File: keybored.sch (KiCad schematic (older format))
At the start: 161 parts, among them J1 USB_C_Receptacle_USB2.0, K1 KEYSW, K10 KEYSW, K11 KEYSW, K12 KEYSW, K13 KEYSW, K14 KEYSW, K15 KEYSW, K16 KEYSW, K17 KEYSW, K18 KEYSW, K19 KEYSW, K2 KEYSW, K20 KEYSW, K21 KEYSW, K22 KEYSW, K23 KEYSW, K24 KEYSW, K25 KEYSW, K26 KEYSW, K27 KEYSW, K28 KEYSW, K29 KEYSW, K3 KEYSW, K30 KEYSW, K31 KEYSW, K32 KEYSW, K33 KEYSW, K34 KEYSW, K35 KEYSW, K36 KEYSW, K37 KEYSW, K38 KEYSW, K39 KEYSW, K4 KEYSW, K40 KEYSW, K41 KEYSW, K43 KEYSW, K44 KEYSW, K45 KEYSW, K46 KEYSW, K47 KEYSW, K48 KEYSW, K49 KEYSW, K5 KEYSW, K50 KEYSW, K51 KEYSW, K52 KEYSW, K53 KEYSW, K54 KEYSW, K57 KEYSW, K58 KEYSW, K59 KEYSW, K6 KEYSW, K60 KEYSW, K61 KEYSW, K62 KEYSW, K63 KEYSW, K64 KEYSW, K65 KEYSW, K66 KEYSW, K67 KEYSW, K68 KEYSW, K69 KEYSW, K7 KEYSW, K8 KEYSW, K9 KEYSW, SW1 SW_PUSH, SW2 Rot_Enc_Sw, U1 ATMEGA32U4, U2 SSD1306-Display_Graphic, Y1 Crystal

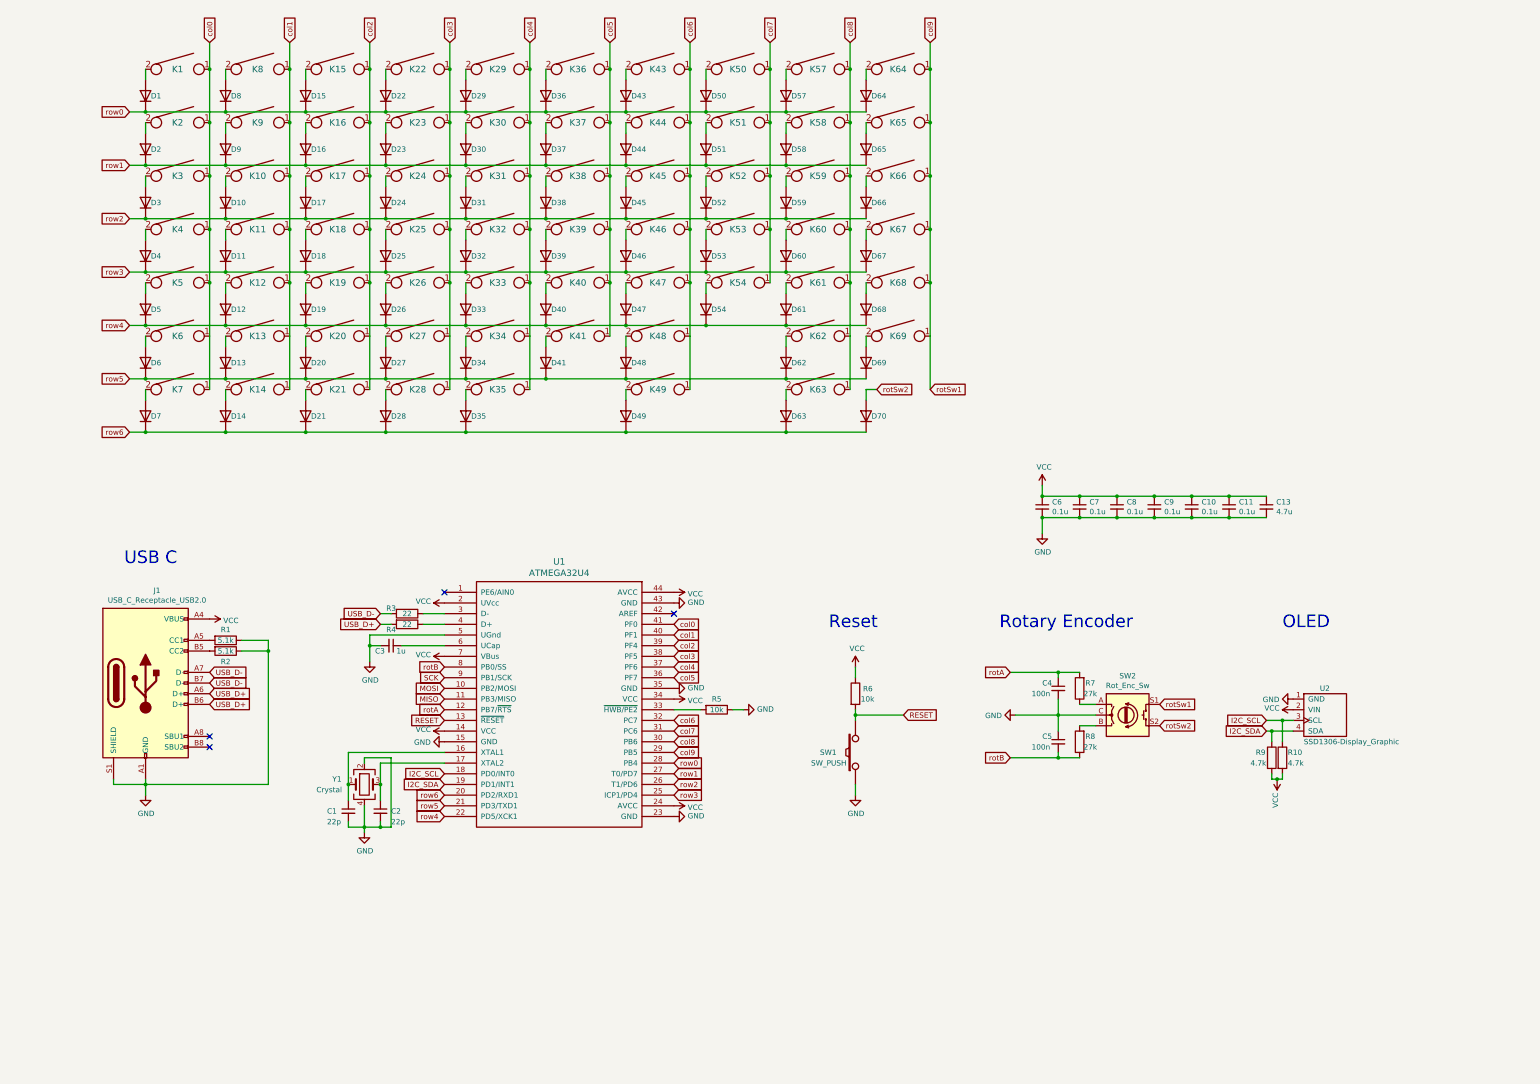
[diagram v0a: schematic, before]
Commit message: Major pcb changes
- now uses a dual footprint for switches
- added ARGB support
- added stabilizer holes
- added header pin support for ISP
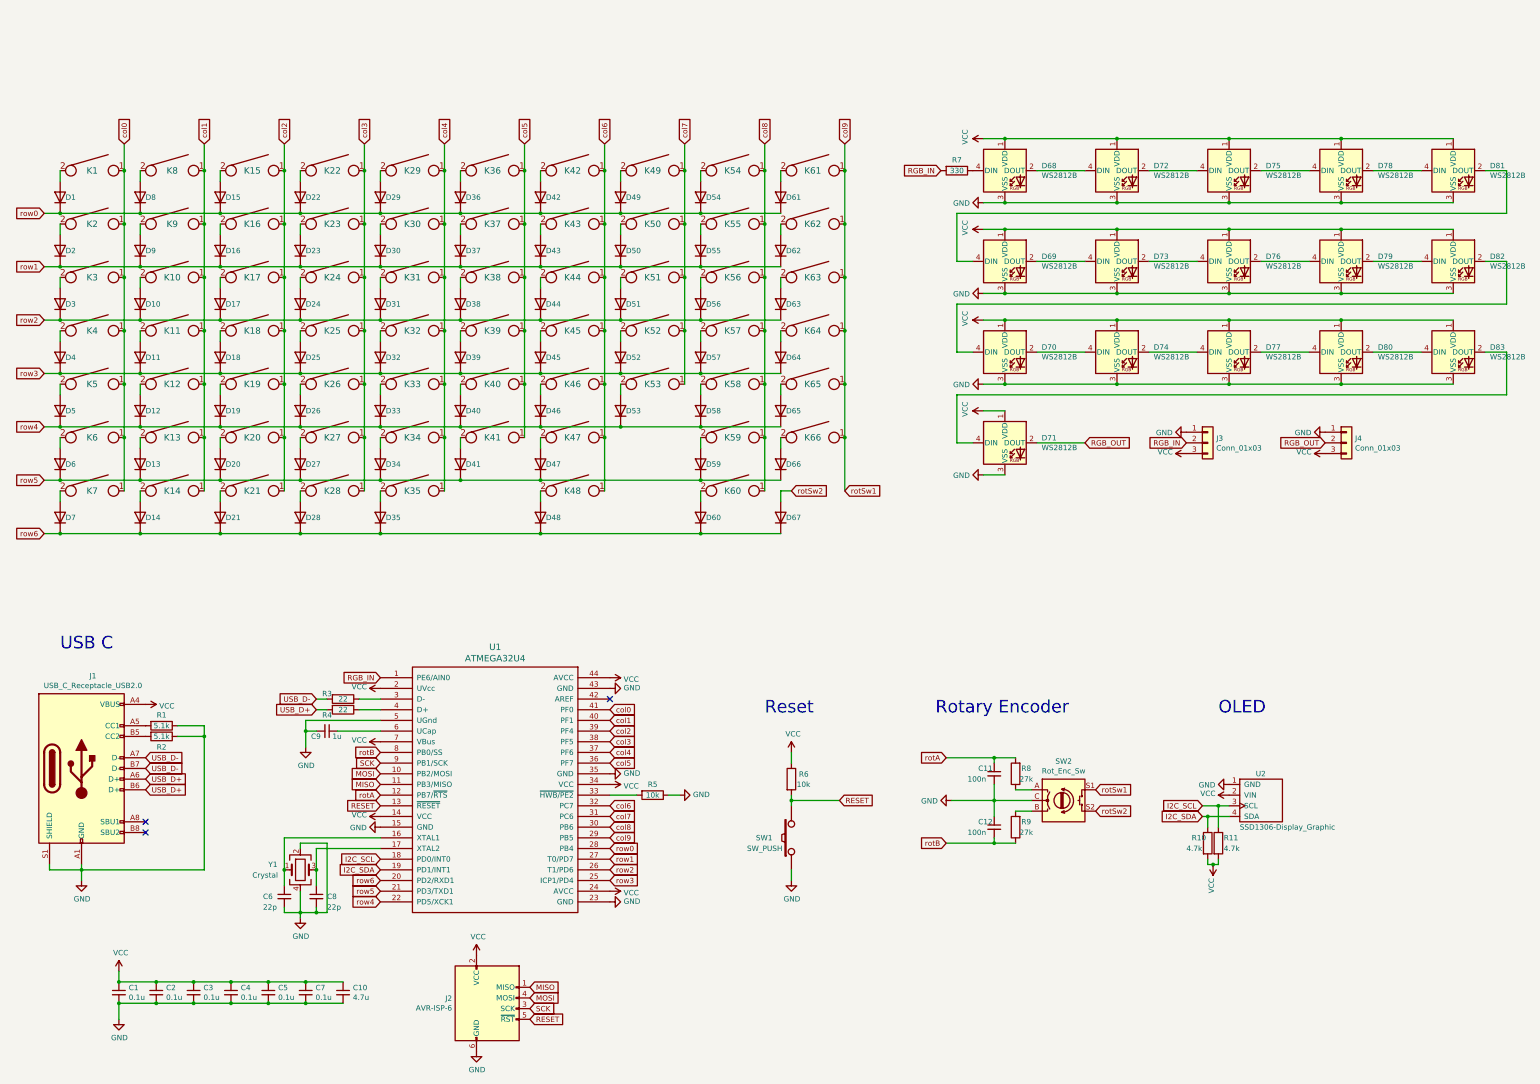
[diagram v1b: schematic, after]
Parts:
- added D68, D69, D70, D71, D72, D73, D74, D75, D76, D77, D78, D79, D80, D81, D82, D83: WS2812B, LED_SMD:LED_WS2812B_PLCC4_5.0x5.0mm_P3.2mm, symbol LED:WS2812B
- added J2: AVR-ISP-6, Connector_PinHeader_2.54mm:PinHeader_2x03_P2.54mm_Vertical, symbol Connector:AVR-ISP-6
- added J3, J4: Conn_01x03, Connector_PinHeader_2.54mm:PinHeader_1x03_P2.54mm_Vertical, symbol Connector_Generic:Conn_01x03
- added R7: 330, Resistor_SMD:R_0805_2012Metric_Pad1.15x1.40mm_HandSolder, symbol Device:R
- K1, K10, K11, K12, K13, K14, K15, K16, K17, K18, K19, K2, K20, K21, K22, K23, K24, K25, K26, K27, K28, K29, K3, K30, K31, K32, K33, K34, K35, K36, K37, K38, K39, K4, K40, K41, K5, K6, K7, K8, K9: footprint keyswitches:Kailh_socket_MX -> keyswitches:Kailh_socket_MX_optional
- K42: renamed from K43; footprint keyswitches:Kailh_socket_MX -> keyswitches:Kailh_socket_MX_optional
- K43: renamed from K44; footprint keyswitches:Kailh_socket_MX -> keyswitches:Kailh_socket_MX_optional
- K44: renamed from K45; footprint keyswitches:Kailh_socket_MX -> keyswitches:Kailh_socket_MX_optional
- K45: renamed from K46; footprint keyswitches:Kailh_socket_MX -> keyswitches:Kailh_socket_MX_optional
- K46: renamed from K47; footprint keyswitches:Kailh_socket_MX -> keyswitches:Kailh_socket_MX_optional
- K47: renamed from K48; footprint keyswitches:Kailh_socket_MX -> keyswitches:Kailh_socket_MX_optional
- K48: renamed from K49; footprint keyswitches:Kailh_socket_MX -> keyswitches:Kailh_socket_MX_optional
- K49: renamed from K50; footprint keyswitches:Kailh_socket_MX -> keyswitches:Kailh_socket_MX_optional
- K50: renamed from K51; footprint keyswitches:Kailh_socket_MX -> keyswitches:Kailh_socket_MX_optional
- K51: renamed from K52; footprint keyswitches:Kailh_socket_MX -> keyswitches:Kailh_socket_MX_optional
- K52: renamed from K53; footprint keyswitches:Kailh_socket_MX -> keyswitches:Kailh_socket_MX_optional
- K53: renamed from K54; footprint keyswitches:Kailh_socket_MX -> keyswitches:Kailh_socket_MX_optional
- K54: renamed from K57; footprint keyswitches:Kailh_socket_MX -> keyswitches:Kailh_socket_MX_optional
- K55: renamed from K58; footprint keyswitches:Kailh_socket_MX -> keyswitches:Kailh_socket_MX_optional
- K56: renamed from K59; footprint keyswitches:Kailh_socket_MX -> keyswitches:Kailh_socket_MX_optional
- K57: renamed from K60; footprint keyswitches:Kailh_socket_MX -> keyswitches:Kailh_socket_MX_optional
- K58: renamed from K61; footprint keyswitches:Kailh_socket_MX -> keyswitches:Kailh_socket_MX_optional
- K59: renamed from K62; footprint keyswitches:Kailh_socket_MX -> keyswitches:Kailh_socket_MX_optional
- K60: renamed from K63; footprint keyswitches:Kailh_socket_MX -> keyswitches:Kailh_socket_MX_optional
- K61: renamed from K64; footprint keyswitches:Kailh_socket_MX -> keyswitches:Kailh_socket_MX_optional
- K62: renamed from K65; footprint keyswitches:Kailh_socket_MX -> keyswitches:Kailh_socket_MX_optional
- K63: renamed from K66; footprint keyswitches:Kailh_socket_MX -> keyswitches:Kailh_socket_MX_optional
- K64: renamed from K67; footprint keyswitches:Kailh_socket_MX -> keyswitches:Kailh_socket_MX_optional
- K65: renamed from K68; footprint keyswitches:Kailh_socket_MX -> keyswitches:Kailh_socket_MX_optional
- K66: renamed from K69; footprint keyswitches:Kailh_socket_MX -> keyswitches:Kailh_socket_MX_optional
- renumbered C6 to C1, C13 to C10, C4 to C11, C5 to C12, C7 to C2, C8 to C3, C9 to C4, C10 to C5, C1 to C6, C11 to C7, C2 to C8, C3 to C9, D43 to D42, D44 to D43, D45 to D44, D46 to D45, D47 to D46, D48 to D47, D49 to D48, D50 to D49, D51 to D50, D52 to D51, D53 to D52, D54 to D53, D57 to D54, D58 to D55, D59 to D56, D60 to D57, D61 to D58, D62 to D59, D63 to D60, D64 to D61, D65 to D62, D66 to D63, D67 to D64, D68 to D65, D69 to D66, D70 to D67, R9 to R10, R10 to R11, R7 to R8, R8 to R9
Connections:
- net GND: now also D68.3 (VSS), D69.3 (VSS), D70.3 (VSS), D71.3 (VSS), D72.3 (VSS), D73.3 (VSS), D74.3 (VSS), D75.3 (VSS), D76.3 (VSS), D77.3 (VSS), D78.3 (VSS), D79.3 (VSS), D80.3 (VSS), D81.3 (VSS), D82.3 (VSS), D83.3 (VSS), J2.6 (GND), J3.1 (Pin_1), J4.1 (Pin_1)
- net MISO: now also J2.1 (MISO)
- net MOSI: now also J2.4 (MOSI)
- net RESET: now also J2.5 (~RST)
- net SCK: now also J2.3 (SCK)
- net VCC: now also D68.1 (VDD), D69.1 (VDD), D70.1 (VDD), D71.1 (VDD), D72.1 (VDD), D73.1 (VDD), D74.1 (VDD), D75.1 (VDD), D76.1 (VDD), D77.1 (VDD), D78.1 (VDD), D79.1 (VDD), D80.1 (VDD), D81.1 (VDD), D82.1 (VDD), D83.1 (VDD), J2.2 (VCC), J3.3 (Pin_3), J4.3 (Pin_3)
- net RGB_IN: now reaches U1.1 (PE6/AIN0)
- net RGB_IN: now also J3.2 (Pin_2), R7.2
- new net: D68.2 (DOUT), D72.4 (DIN)
- new net: D68.4 (DIN), R7.1
- new net: D71.4 (DIN), D83.2 (DOUT)
- new net: D72.2 (DOUT), D75.4 (DIN)
- new net: D75.2 (DOUT), D78.4 (DIN)
- new net: D78.2 (DOUT), D81.4 (DIN)
- new net: D69.4 (DIN), D81.2 (DOUT)
- new net: D69.2 (DOUT), D73.4 (DIN)
- new net: D73.2 (DOUT), D76.4 (DIN)
- new net: D76.2 (DOUT), D79.4 (DIN)
- new net: D79.2 (DOUT), D82.4 (DIN)
- new net: D70.4 (DIN), D82.2 (DOUT)
- new net: D70.2 (DOUT), D74.4 (DIN)
- new net: D74.2 (DOUT), D77.4 (DIN)
- new net: D77.2 (DOUT), D80.4 (DIN)
- new net: D80.2 (DOUT), D83.4 (DIN)
- new net RGB_OUT: D71.2 (DOUT), J4.2 (Pin_2)
- no-connect marks 4 -> 3
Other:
- moved on the sheet: C1, C10, C11, C12, C2, C3, C4, C5, C6, C7, C8, C9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

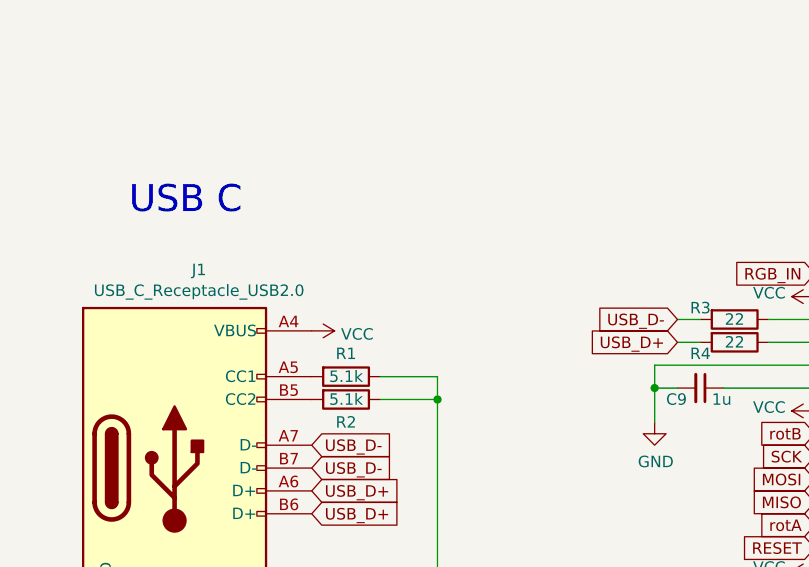
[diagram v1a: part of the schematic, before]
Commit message: Add plate, updates to PCB
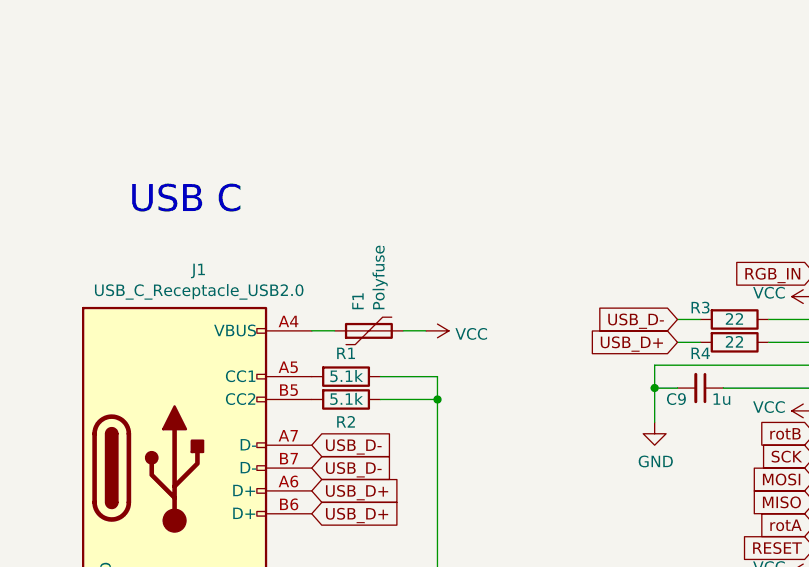
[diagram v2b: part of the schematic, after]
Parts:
- added F1: Polyfuse, symbol Device:Polyfuse
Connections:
- net VCC: now also F1.2; no longer J1.A4 (VBUS), J1.A9 (VBUS), J1.B4 (VBUS), J1.B9 (VBUS)
- new net: F1.1, J1.A4 (VBUS), J1.A9 (VBUS), J1.B4 (VBUS), J1.B9 (VBUS)
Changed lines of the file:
@@
 L power:VCC #PWR04
 U 1 1 5F21B859
-P 2650 7450
-F 0 "#PWR04" H 2650 7300 50  0001 C CNN
-F 1 "VCC" V 2665 7578 50  0000 L CNN
-F 2 "" H 2650 7450 50  0001 C CNN
-F 3 "" H 2650 7450 50  0001 C CNN
-	1    2650 7450
+P 3150 7450
+F 0 "#PWR04" H 3150 7300 50  0001 C CNN
+F 1 "VCC" V 3165 7578 50  0000 L CNN
+F 2 "" H 3150 7450 50  0001 C CNN
+F 3 "" H 3150 7450 50  0001 C CNN
+	1    3150 7450
 	0    1    1    0
 $EndComp
@@
 Wire Wire Line
 	10500 4700 10700 4700
+$Comp
+L Device:Polyfuse F1
+U 1 1 5F57EE3A
+P 2900 7450
+F 0 "F1" H 2988 7496 50  0000 L CNN
+F 1 "Polyfuse" H 2988 7405 50  0000 L CNN
+F 2 "" H 2950 7250 50  0001 L CNN
+F 3 "~" H 2900 7450 50  0001 C CNN
+	1    2900 7450
+	0    -1   -1   0
+$EndComp
+Wire Wire Line
+	2650 7450 2750 7450
+Wire Wire Line
+	3050 7450 3150 7450
 $EndSCHEMATC
